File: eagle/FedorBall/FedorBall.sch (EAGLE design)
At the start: 18 parts, among them IC1 MEGA16-P, IC2 7805T, X1 22-23-2041, X2 22-23-2041

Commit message: update schematic for main board
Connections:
- net BLANK: now also IC1.(OC1B)PD4; no longer IC1.(AIN0/INT2)PB2
- net GSCLK: now also IC1.(OC2)PD7; no longer IC1.(AIN1/OC0)PB3
- net VPRG: now also IC1.(ICP)PD6; no longer IC1.(T1)PB1
- net XLAT: now also IC1.(OC1A)PD5; no longer IC1.(SS)PB4
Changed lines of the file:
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@@
 <net name="BLANK" class="0">
-<segment>
-<pinref part="IC1" gate="G$1" pin="(AIN0/INT2)PB2"/>
-<wire x1="15.24" y1="2.54" x2="27.94" y2="2.54" width="0.1524" layer="91"/>
-<junction x="27.94" y="2.54"/>
-<label x="17.78" y="2.54" size="1.778" layer="95"/>
-</segment>
 <segment>
 <pinref part="LED_DRIVER" gate="G$1" pin="6"/>
@@
 <label x="83.82" y="-20.32" size="1.778" layer="95"/>
 </segment>
+<segment>
+<pinref part="IC1" gate="G$1" pin="(OC1B)PD4"/>
+<wire x1="15.24" y1="-38.1" x2="25.4" y2="-38.1" width="0.1524" layer="91"/>
+<junction x="25.4" y="-38.1"/>
+<label x="17.78" y="-38.1" size="1.778" layer="95"/>
+</segment>
 </net>
 <net name="GSCLK" class="0">
-<segment>
-<pinref part="IC1" gate="G$1" pin="(AIN1/OC0)PB3"/>
-<wire x1="15.24" y1="5.08" x2="27.94" y2="5.08" width="0.1524" layer="91"/>
-<junction x="27.94" y="5.08"/>
-<label x="17.78" y="5.08" size="1.778" layer="95"/>
-</segment>
 <segment>
 <pinref part="LED_DRIVER" gate="G$1" pin="7"/>
@@
 <label x="63.5" y="-22.86" size="1.778" layer="95"/>
 </segment>
+<segment>
+<pinref part="IC1" gate="G$1" pin="(OC2)PD7"/>
+<wire x1="15.24" y1="-30.48" x2="25.4" y2="-30.48" width="0.1524" layer="91"/>
+<junction x="25.4" y="-30.48"/>
+<label x="17.78" y="-30.48" size="1.778" layer="95"/>
+</segment>
 </net>
 <net name="VPRG" class="0">
-<segment>
-<pinref part="IC1" gate="G$1" pin="(T1)PB1"/>
-<wire x1="15.24" y1="0" x2="27.94" y2="0" width="0.1524" layer="91"/>
-<junction x="27.94" y="0"/>
-<label x="17.78" y="0" size="1.778" layer="95"/>
-</segment>
 <segment>
 <pinref part="LED_DRIVER" gate="G$1" pin="5"/>
@@
 <junction x="60.96" y="-20.32"/>
 <label x="63.5" y="-20.32" size="1.778" layer="95"/>
+</segment>
+<segment>
+<pinref part="IC1" gate="G$1" pin="(ICP)PD6"/>
+<wire x1="15.24" y1="-33.02" x2="25.4" y2="-33.02" width="0.1524" layer="91"/>
+<junction x="25.4" y="-33.02"/>
+<label x="17.78" y="-33.02" size="1.778" layer="95"/>
 </segment>
 </net>
@@
 <net name="XLAT" class="0">
 <segment>
-<pinref part="IC1" gate="G$1" pin="(SS)PB4"/>
-<wire x1="15.24" y1="7.62" x2="27.94" y2="7.62" width="0.1524" layer="91"/>
-<junction x="27.94" y="7.62"/>
-<label x="17.78" y="7.62" size="1.778" layer="95"/>
-</segment>
-<segment>
 <pinref part="LED_DRIVER" gate="G$1" pin="3"/>
 <wire x1="68.58" y1="-17.78" x2="60.96" y2="-17.78" width="0.1524" layer="91"/>
@@
 <label x="63.5" y="-17.78" size="1.778" layer="95"/>
 </segment>
+<segment>
+<pinref part="IC1" gate="G$1" pin="(OC1A)PD5"/>
+<wire x1="15.24" y1="-35.56" x2="25.4" y2="-35.56" width="0.1524" layer="91"/>
+<junction x="25.4" y="-35.56"/>
+<label x="17.78" y="-35.56" size="1.778" layer="95"/>
+</segment>
 </net>

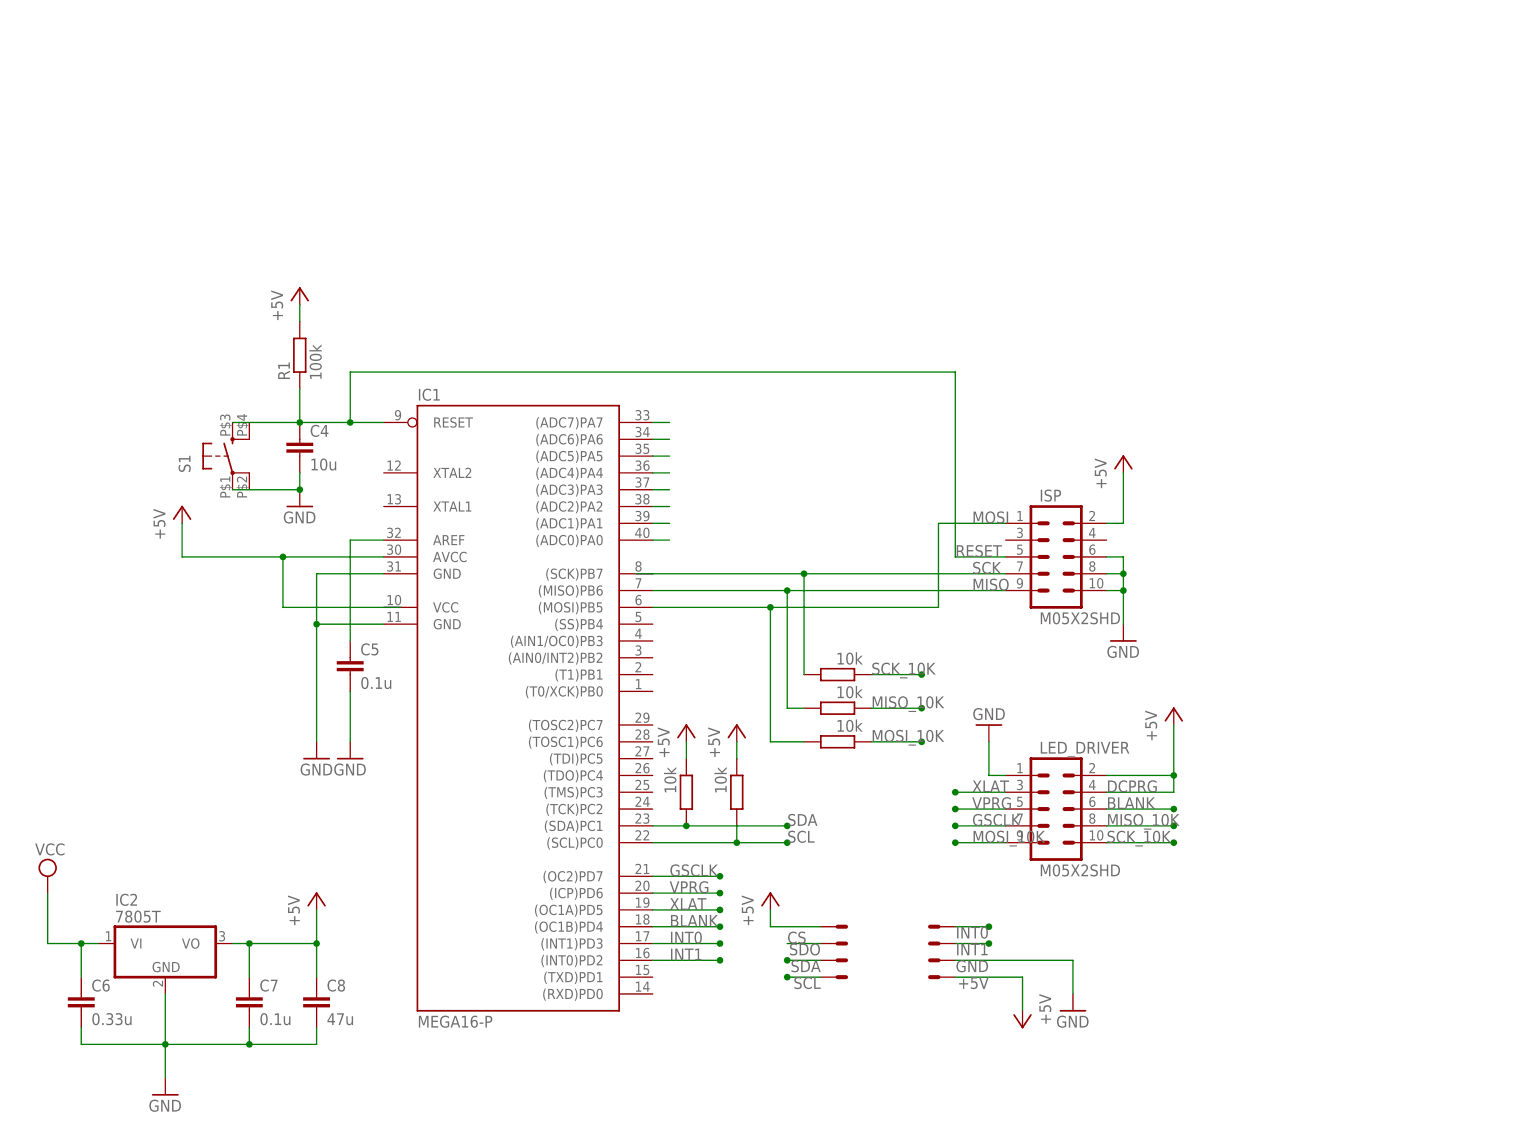
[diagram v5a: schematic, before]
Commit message: update schematic and board according to last hardware experiments
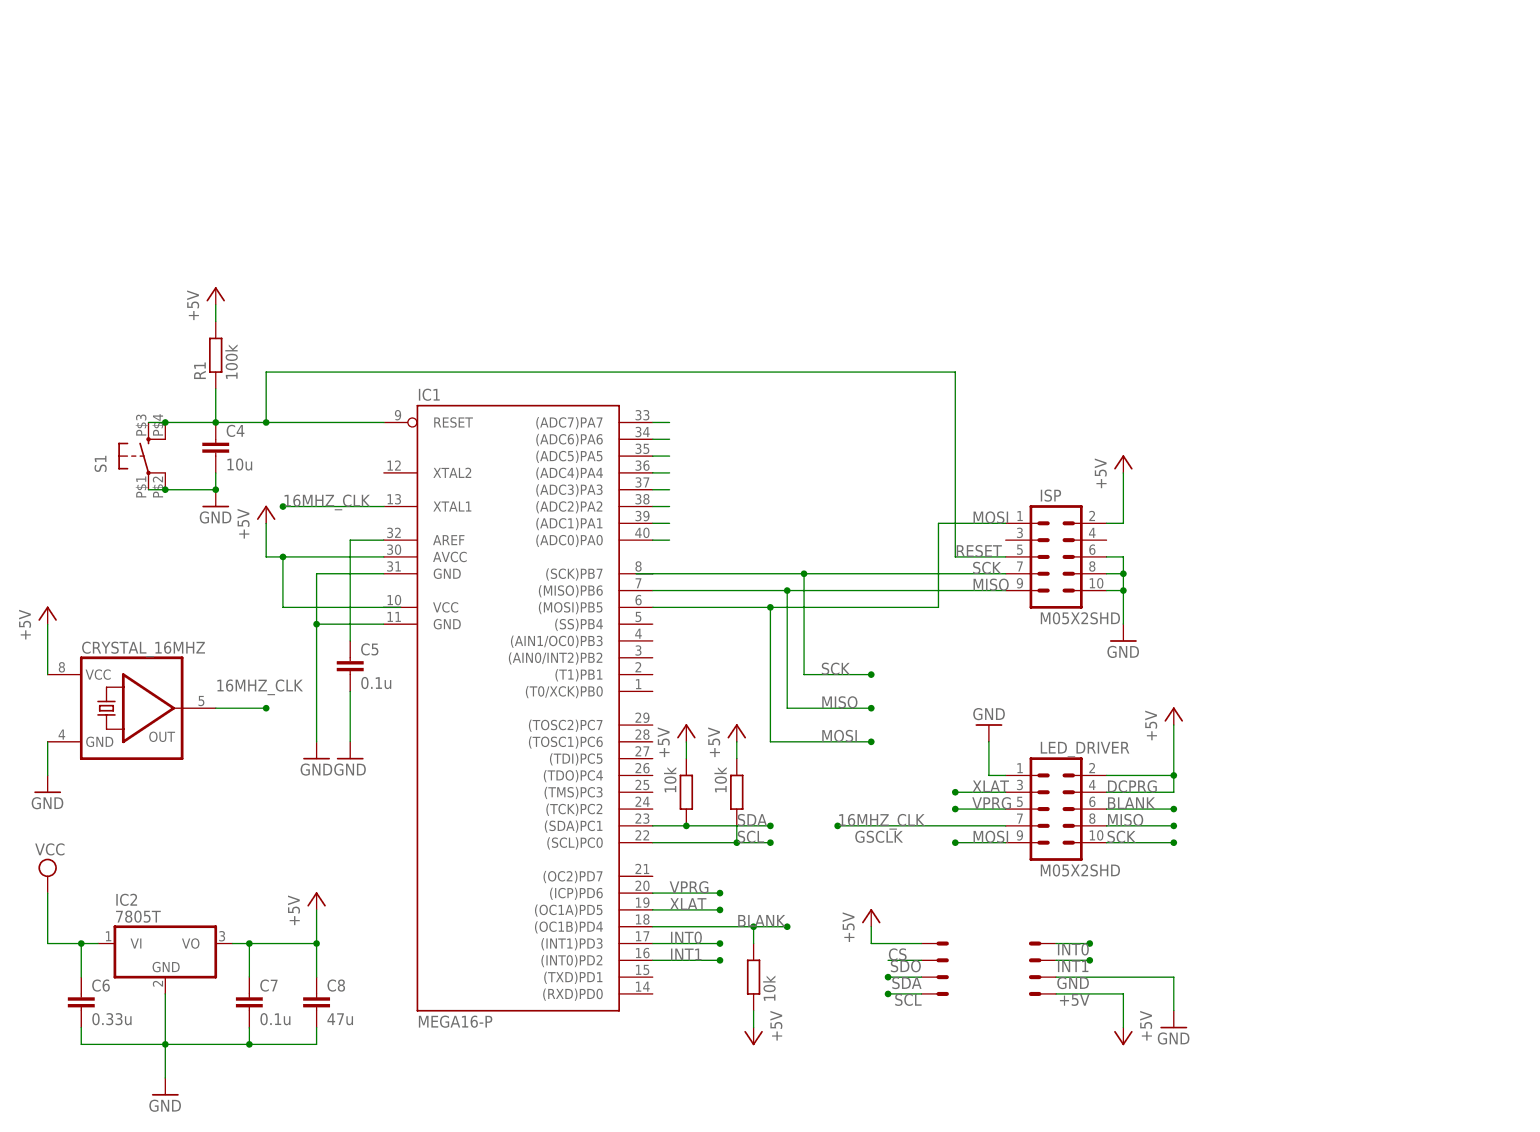
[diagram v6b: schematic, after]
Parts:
- removed R3, R4: 10k, rcl:R-EU_0207/10
- added CRYSTAL_16MHZ: (no value), crystal:QG5460
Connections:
- removed net GSCLK: IC1.(OC2)PD7, LED_DRIVER.7
- removed net MISO_10K: LED_DRIVER.8, R3.1
- removed net MOSI_10K: LED_DRIVER.9, R4.1
- removed net N$5: IC1.(MOSI)PB5, ISP.1, R4.2
- removed net N$7: IC1.(SCK)PB7, ISP.7, R2.2
- removed net N$8: IC1.(MISO)PB6, ISP.9, R3.2
- removed net SCK_10K: LED_DRIVER.10, R2.1
- new net 16MHZ_CLK: CRYSTAL_16MHZ.OUT, IC1.XTAL1, LED_DRIVER.7
- new net MISO: IC1.(MISO)PB6, ISP.9, LED_DRIVER.8
- new net MOSI: IC1.(MOSI)PB5, ISP.1, LED_DRIVER.9
- new net SCK: IC1.(SCK)PB7, ISP.7, LED_DRIVER.10
- net +5V: now also CRYSTAL_16MHZ.VCC, R2.1
- net BLANK: now also R2.2
- net GND: now also CRYSTAL_16MHZ.GND, S1.2
- net N$6: now also S1.4
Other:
- note added: "GSCLK"
- moved on the sheet: C4, R1, S1

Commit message: minor scheme changes
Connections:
- net INT0: now also IC1.(INT0)PD2; no longer IC1.(INT1)PD3
- net INT1: now also IC1.(INT1)PD3; no longer IC1.(INT0)PD2
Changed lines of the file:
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@@
 <net name="INT1" class="0">
+<segment>
+<pinref part="X1" gate="-3" pin="S"/>
+<wire x1="76.2" y1="-43.18" x2="81.28" y2="-43.18" width="0.1524" layer="91"/>
+<label x="81.28" y="-43.18" size="1.778" layer="95" rot="R180"/>
+<junction x="81.28" y="-43.18"/>
+</segment>
+<segment>
+<pinref part="IC1" gate="G$1" pin="(INT1)PD3"/>
+<wire x1="15.24" y1="-40.64" x2="25.4" y2="-40.64" width="0.1524" layer="91"/>
+<junction x="25.4" y="-40.64"/>
+<label x="17.78" y="-40.64" size="1.778" layer="95"/>
+</segment>
+</net>
+<net name="INT0" class="0">
+<segment>
+<pinref part="X1" gate="-4" pin="S"/>
+<wire x1="76.2" y1="-40.64" x2="81.28" y2="-40.64" width="0.1524" layer="91"/>
+<label x="81.28" y="-40.64" size="1.778" layer="95" rot="R180"/>
+<junction x="81.28" y="-40.64"/>
+</segment>
 <segment>
 <pinref part="IC1" gate="G$1" pin="(INT0)PD2"/>
@@
 <label x="17.78" y="-43.18" size="1.778" layer="95"/>
 </segment>
-<segment>
-<pinref part="X1" gate="-3" pin="S"/>
-<wire x1="76.2" y1="-43.18" x2="81.28" y2="-43.18" width="0.1524" layer="91"/>
-<label x="81.28" y="-43.18" size="1.778" layer="95" rot="R180"/>
-<junction x="81.28" y="-43.18"/>
-</segment>
 </net>
-<net name="INT0" class="0">
-<segment>
-<pinref part="IC1" gate="G$1" pin="(INT1)PD3"/>
-<wire x1="15.24" y1="-40.64" x2="25.4" y2="-40.64" width="0.1524" layer="91"/>
-<junction x="25.4" y="-40.64"/>
-<label x="17.78" y="-40.64" size="1.778" layer="95"/>
-</segment>
-<segment>
-<pinref part="X1" gate="-4" pin="S"/>
-<wire x1="76.2" y1="-40.64" x2="81.28" y2="-40.64" width="0.1524" layer="91"/>
-<label x="81.28" y="-40.64" size="1.778" layer="95" rot="R180"/>
-<junction x="81.28" y="-40.64"/>
-</segment>
-</net>
